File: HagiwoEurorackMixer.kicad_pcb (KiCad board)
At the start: 2 copper layers, 29 x 106 mm, 22 parts, among them J1 IN1, J2 IN2, J3 IN3, J4 IN4, J5 OUT, J7 Eurorack_Power_10pin_Unshroud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, U2 TL072

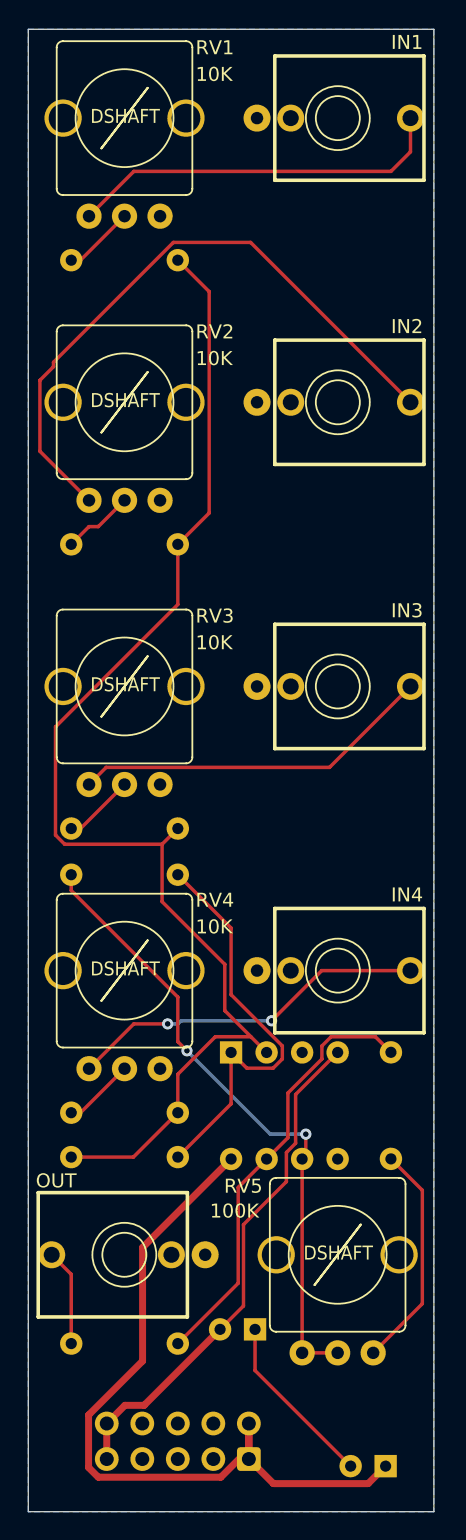
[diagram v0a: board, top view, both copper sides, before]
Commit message: laid out V1.1 again for better placement
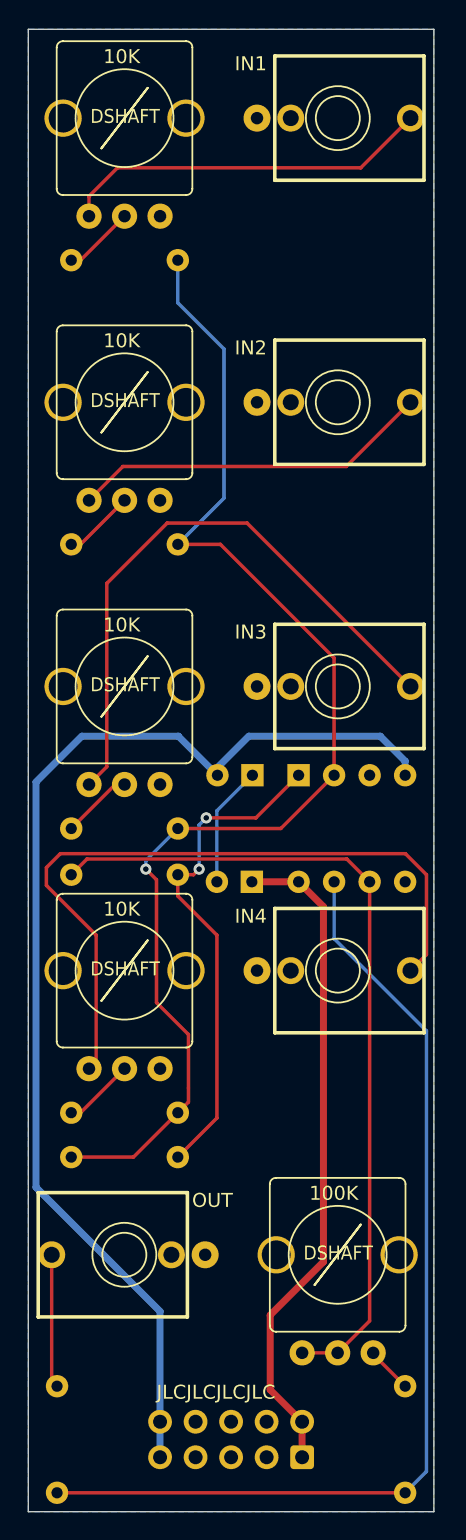
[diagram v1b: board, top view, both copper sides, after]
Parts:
- J1, J2, J3, J4, J5: footprint LibraryAll:EighthInch_PJ398SM_T_TN_S -> Library:EighthInch_PJ398SM_T_TN_S
- J7: footprint LibraryAll:IDC-Header_2x05_P2.54mm_Vertical_Euro_Power_Striped -> Library:IDC-Header_2x05_P2.54mm_Vertical_Euro_Power_Striped
- RV1, RV2, RV3, RV4: footprint LibraryAll:Pot_9mm_DShaft_RemovedPins4_5 -> Library:Pot_9mm_DShaft_RemovedPins4_5
- moved C1 42.9 mm to (92.6, 114.1)
- moved C2 39.6 mm to (92.7, 106.5)
- moved U2 20.4 mm to (96.0, 106.5)
- moved R7 16.3 mm to (103.6, 150.2), turned to -90 degrees
- moved R8 13.7 mm to (78.7, 157.8), turned to 90 degrees
- moved J7 3.81 mm to (96.2, 155.3)
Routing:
- net Net-(U2C-V-): track 36.7 -> 84.1 mm
- net Net-(R7-Pad2): track 31.2 -> 71.9 mm
- net Net-(J4-PadT): track 25.9 -> 51.6 mm, vias 2 -> 0
- net Net-(J2-PadT): track 45.5 -> 25.9 mm
- net Net-(J3-PadT): track 25.9 -> 43.2 mm
- net Net-(U2B--): track 45.3 -> 59.6 mm, vias 2 -> 0
- net Net-(R7-Pad1): track 16.3 -> 3.33 mm
- net Net-(U2C-V+): track 54.3 -> 47.8 mm
- net Net-(R5-Pad2): track 29.7 -> 35.9 mm, vias 0 -> 2
- net Net-(C1-Pad2): track 12.6 -> 8.67 mm
- net Net-(J5-PadT): track 6.93 -> 9.56 mm
- net Net-(U2A--): track 92.1 -> 90.5 mm, vias 0 -> 1
- net Net-(J1-PadT): track 27.3 -> 26.7 mm
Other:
- board text added: "CONCRETE MIXER"
- board text added: "INSPIRED BY HAGIWO + DOEPFER DESIGNS"
- board text added: "JLCJLCJLCJLC"
- board text added: "PCB BY 42 BERLIN SYNTHLAB"
- board text added: "SynthLab"
- board text added: "V1.1"
- board text added: "github.com/fablabnk/SynthLabProjects"
- board text removed: "BY 42 BERLIN SYNTHLAB https://github.com/fablabnk/"
- board text removed: "CONCRETE MIXER V1.1"
- board text removed: "ORIGINAL DESIGN BY HAGIWO / DOEPFER"

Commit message: laid out V1.1 again for better placement
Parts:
- RV5: footprint LibraryAll:Pot_9mm_DShaft_RemovedPins4_5 -> Library:Pot_9mm_DShaft_RemovedPins4_5
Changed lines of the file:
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@@
 		)
 	)
-	(footprint "LibraryAll:Pot_9mm_DShaft_RemovedPins4_5"
+	(footprint "Library:Pot_9mm_DShaft_RemovedPins4_5"
 		(layer "F.Cu")
 		(at 98.78 140.79 180)
@@
 			)
 		)
-		(property "Footprint" "LibraryAll:Pot_9mm_DShaft_RemovedPins4_5"
+		(property "Footprint" "Library:Pot_9mm_DShaft_RemovedPins4_5"
 			(at 0 0 180)
 			(unlocked yes)

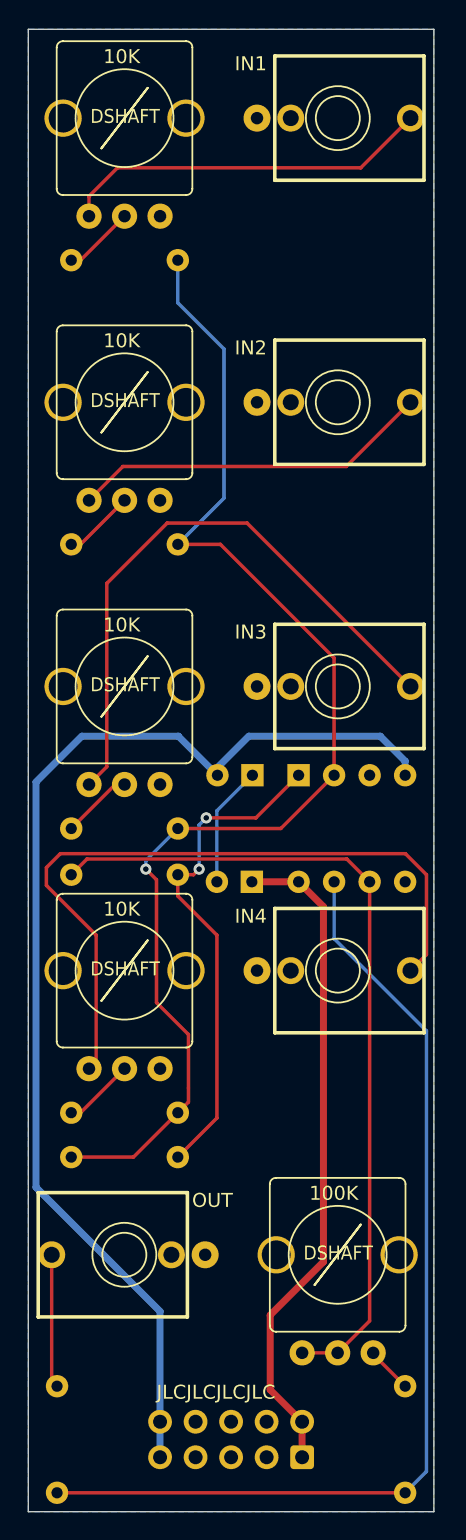
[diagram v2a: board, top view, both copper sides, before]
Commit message: moved decoupling caps back near power rails - now really ready for V1.1 production
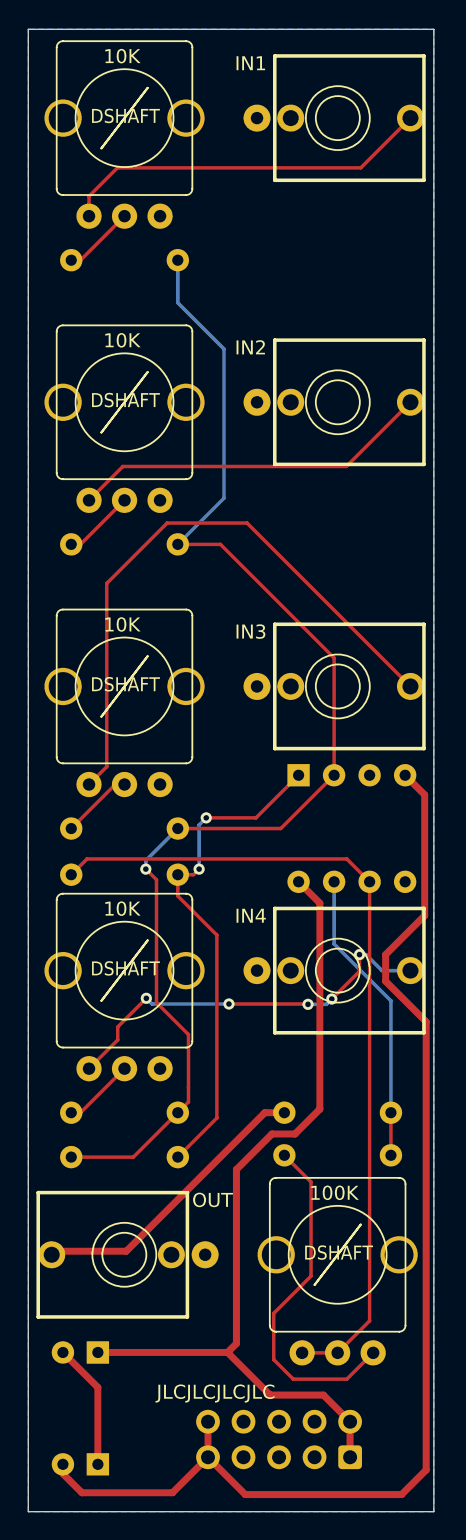
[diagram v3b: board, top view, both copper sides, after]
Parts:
- moved C2 50.5 mm to (81.6, 155.8)
- moved R8 36.2 mm to (102.6, 130.6), turned to 180 degrees
- moved C1 35.4 mm to (81.6, 147.8)
- moved R7 18.6 mm to (95.0, 133.7), turned to 0 degrees
- moved J7 3.43 mm to (99.7, 155.3)
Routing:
- net Net-(R7-Pad2): track 71.9 -> 21.2 mm
- net Net-(J4-PadT): track 51.6 -> 28.4 mm, vias 0 -> 5
- net Net-(R7-Pad1): track 3.33 -> 25.1 mm
- net Net-(U2C-V+): track 47.8 -> 60.6 mm
- net Net-(J5-PadT): track 9.56 -> 20.8 mm
- net Net-(U2C-V-): track 84.1 -> 85.3 mm

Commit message: realised pots and jacks were mirrored horizontally across the whole pcb - reworked and rerouted still for V1.1 - with production files
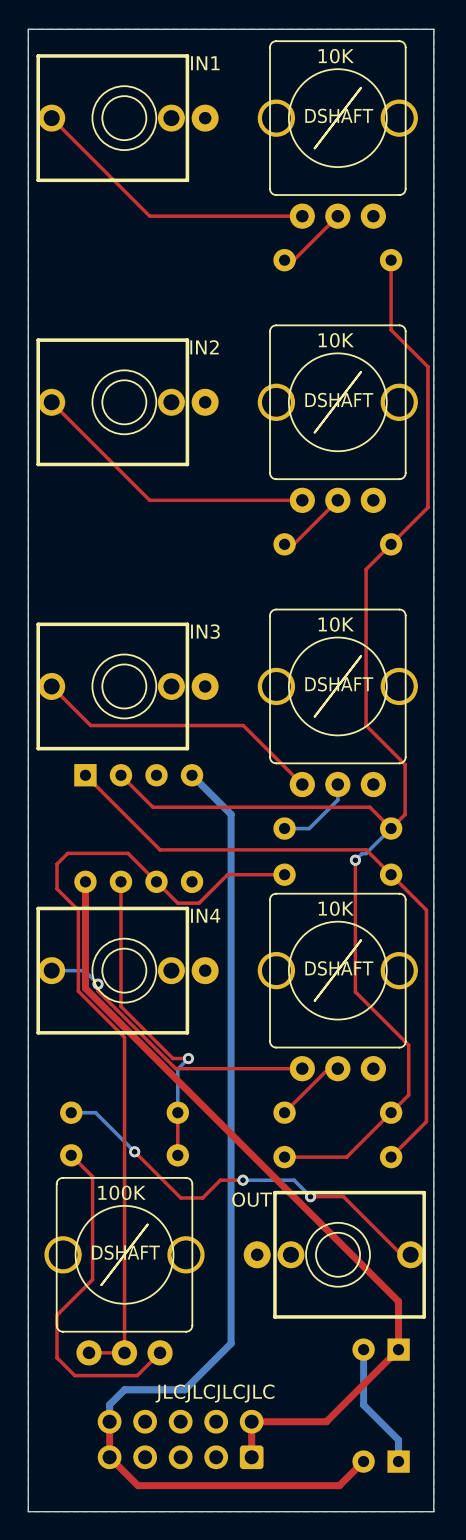
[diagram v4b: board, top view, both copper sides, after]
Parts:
- moved C1 21.5 mm to (103.1, 147.6)
- moved C2 21.5 mm to (103.1, 155.6)
- moved R6 15.3 mm to (102.6, 113.6)
- moved J5 15.3 mm to (98.8, 140.8), turned to 180 degrees
- moved R1 15.3 mm to (95.0, 69.7)
- moved R2 15.3 mm to (95.0, 90.0)
- moved R3 15.3 mm to (95.0, 110.3)
- moved R4 15.3 mm to (95.0, 130.6)
- moved R5 15.3 mm to (95.0, 133.8)
- moved RV1 15.3 mm to (98.8, 59.5)
- moved RV2 15.3 mm to (98.8, 79.8)
- moved RV3 15.3 mm to (98.8, 100.2)
- moved RV4 15.3 mm to (98.8, 120.5)
- moved R8 15.2 mm to (87.4, 130.6)
- moved U2 15.2 mm to (80.7, 106.5)
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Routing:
- net Net-(J3-PadT): track 43.2 -> 20.8 mm
- net Net-(R5-Pad2): track 35.9 -> 47.1 mm, vias 2 -> 0
- net Net-(U2C-V-): track 85.3 -> 75.8 mm
- net Net-(J5-PadT): track 20.8 -> 29.5 mm, vias 0 -> 3
- net Net-(U2A--): track 90.5 -> 98.6 mm
- net Net-(J4-PadT): track 28.4 -> 21.1 mm, vias 5 -> 1
- net Net-(J1-PadT): track 26.7 -> 20.8 mm
- net Net-(J2-PadT): track 25.9 -> 20.8 mm
- net Net-(U2C-V+): track 60.6 -> 57.9 mm
- net Net-(R7-Pad2): track 21.2 -> 22.5 mm, vias 0 -> 1
- net Net-(U2B--): track 59.6 -> 58.4 mm
- net Net-(R3-Pad1): track 5.11 -> 5.76 mm
